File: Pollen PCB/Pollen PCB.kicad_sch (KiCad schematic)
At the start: 4 parts, among them U1 DS18B20, U2 Pico, U3 GY-NEO6MV2

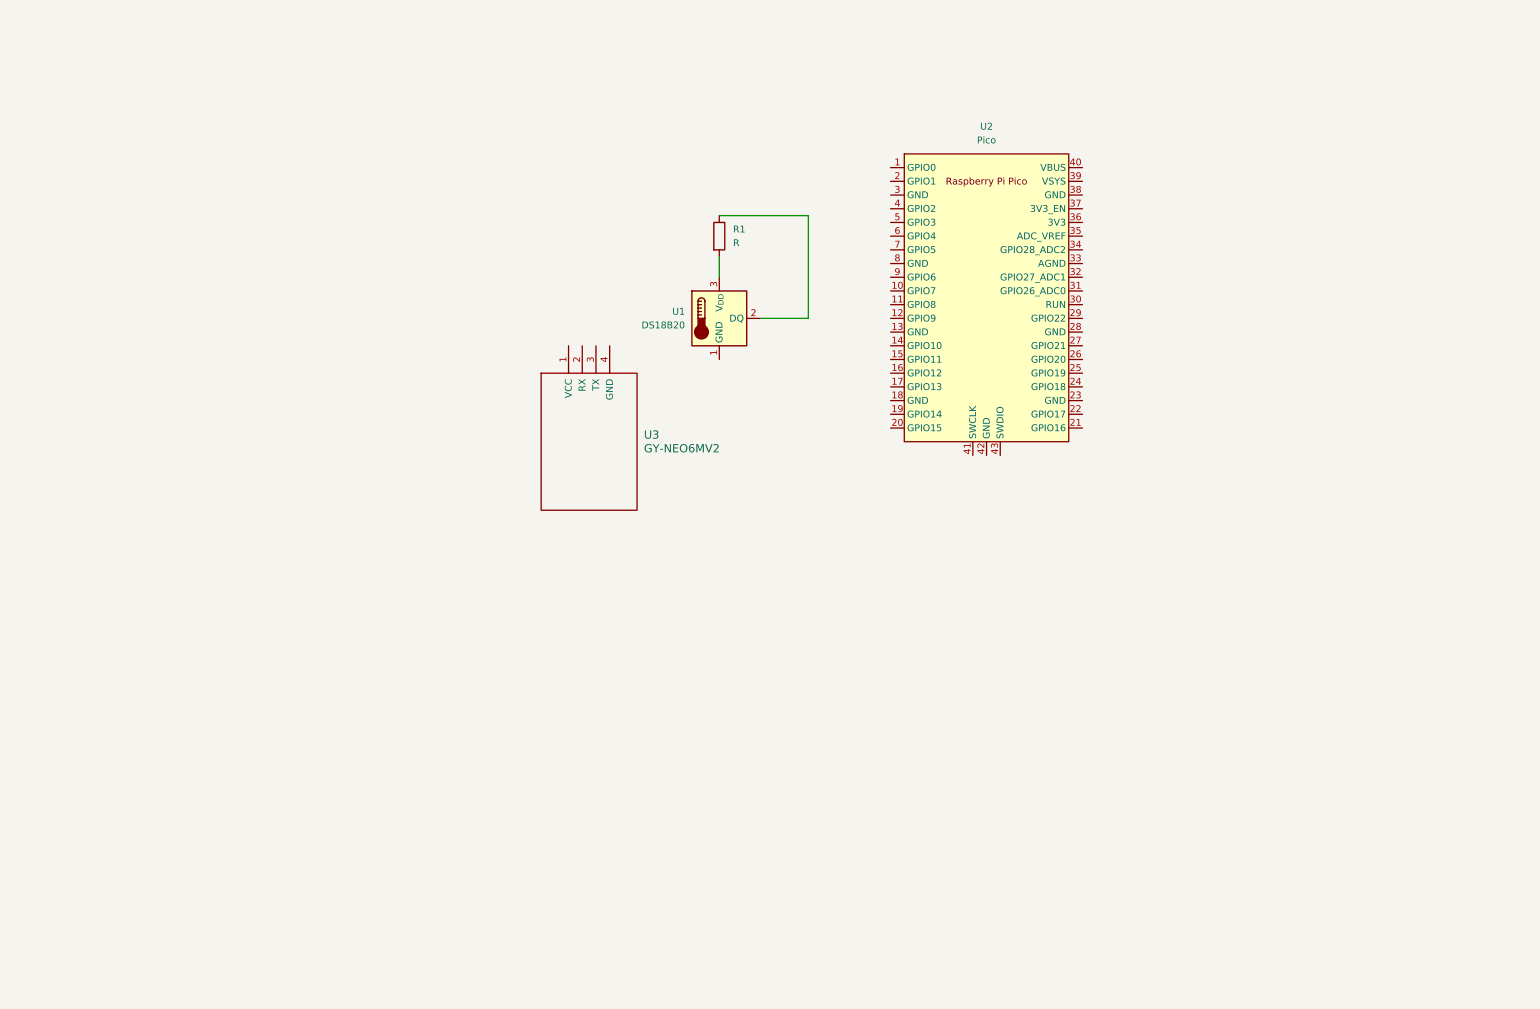
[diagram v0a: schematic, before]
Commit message: Start drawing the schematic
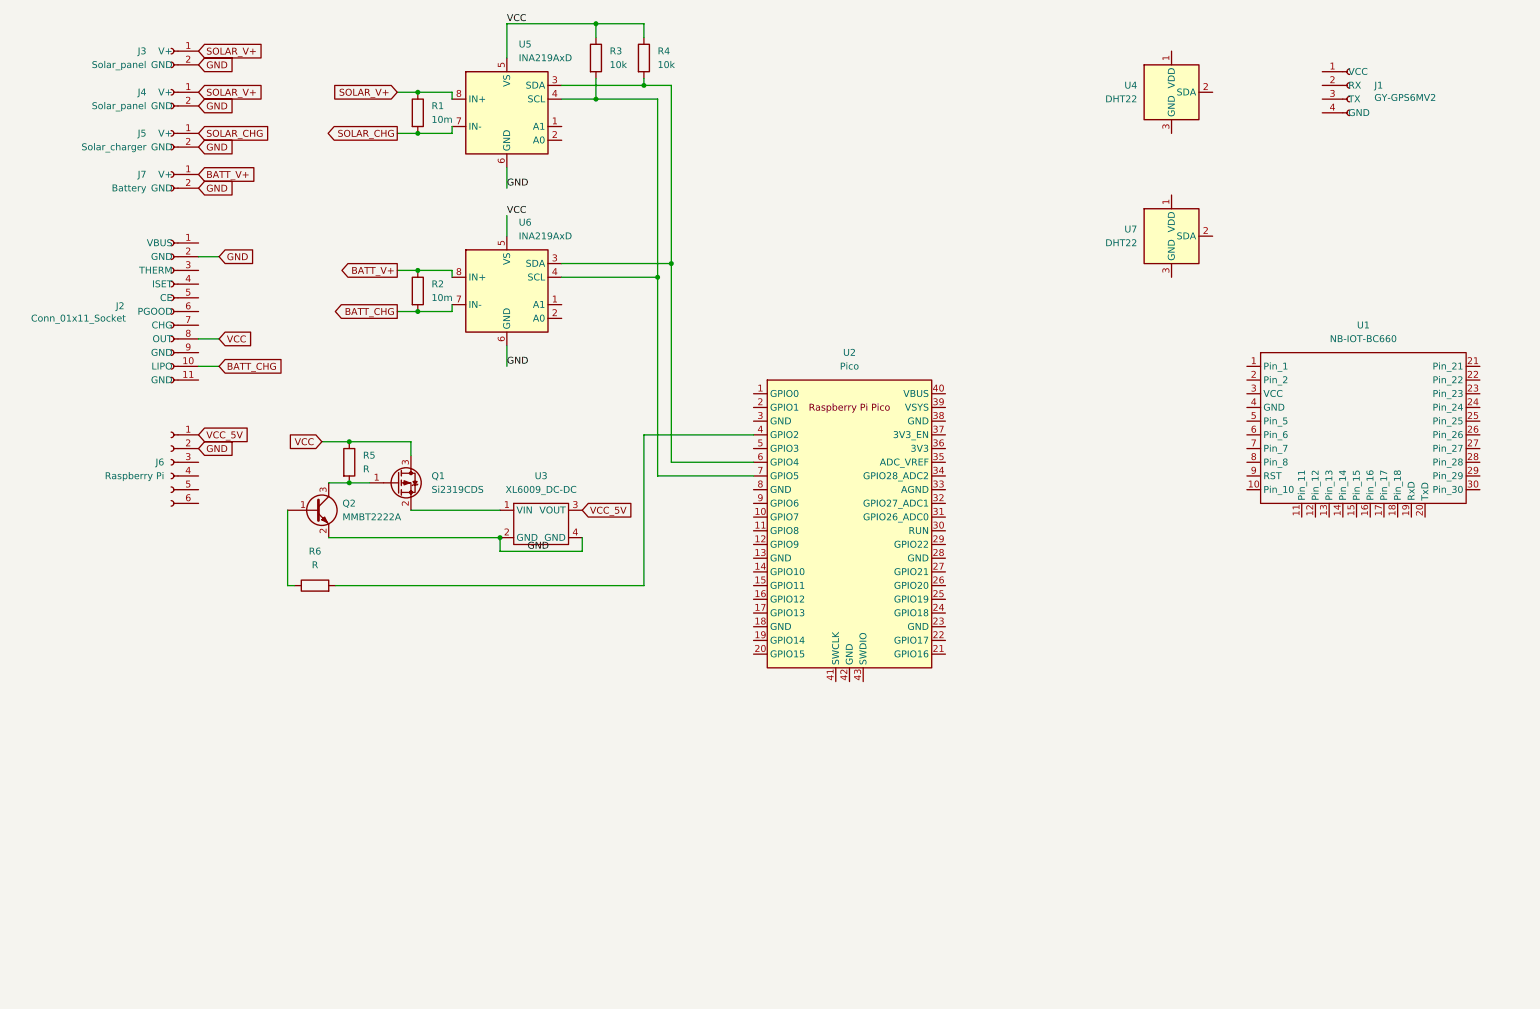
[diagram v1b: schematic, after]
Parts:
- removed U1: DS18B20, Package_TO_SOT_THT:TO-92_Inline, symbol Sensor_Temperature:DS18B20
- removed U3: GY-NEO6MV2, symbol megasaturnv_custom_components:GY-NEO6MV2
- added J1: GY-GPS6MV2, Connector_PinSocket_2.54mm:PinSocket_1x04_P2.54mm_Vertical, symbol Connector:Conn_01x04_Socket
- added J2: Conn_01x11_Socket, Connector_PinSocket_2.54mm:PinSocket_1x11_P2.54mm_Vertical, symbol Connector:Conn_01x11_Socket
- added J3, J4: Solar_panel, Connector_PinSocket_2.54mm:PinSocket_1x02_P2.54mm_Vertical, symbol Connector:Conn_01x02_Socket
- added J5: Solar_charger, Connector_PinSocket_2.54mm:PinSocket_1x02_P2.54mm_Vertical, symbol Connector:Conn_01x02_Socket
- added J6: Raspberry Pi, Connector_PinSocket_2.54mm:PinSocket_1x06_P2.54mm_Vertical, symbol Connector:Conn_01x06_Socket
- added J7: Battery, Connector_PinSocket_2.54mm:PinSocket_1x02_P2.54mm_Vertical, symbol Connector:Conn_01x02_Socket
- added Q1: Si2319CDS, Package_TO_SOT_SMD:SOT-23, symbol Transistor_FET:Si2319CDS
- added Q2: MMBT2222A, Package_TO_SOT_SMD:SOT-23, symbol Transistor_BJT:MMBT2222A
- added R2: 10m, symbol Device:R
- added R3, R4: 10k, symbol Device:R
- added R5, R6: R, symbol Device:R
- added U1: NB-IOT-BC660, Custom_Components:NB-IOT-BC660, symbol Custom_Components:BC660_Olimex_module
- added U3: XL6009_DC-DC, Custom_Components:XL6009_DC-DC, symbol Custom_Components:XL6009_DC-DC
- added U4, U7: DHT22, Sensor:ASAIR_AM2302_P2.54mm_Vertical, symbol Sensor:AM2302
- added U5, U6: INA219AxD, Package_SO:SOIC-8_3.9x4.9mm_P1.27mm, symbol Sensor_Energy:INA219AxD
- R1: value R -> 10m; footprint Resistor_THT:R_Axial_DIN0204_L3.6mm_D1.6mm_P7.62mm_Horizontal -> (none)
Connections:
- net SOLAR_V+: now reaches R1.1
- net SOLAR_V+: now also J3.1 (V+), J4.1 (V+), U5.8 (IN+)
- net SOLAR_CHG: now reaches R1.2
- net SOLAR_CHG: now also J5.1 (V+), U5.7 (IN-)
- net at U2.4 (GPIO2): now also R6.2
- net at U2.6 (GPIO4): now also R4.2, U5.3 (SDA), U6.3 (SDA)
- net at U2.7 (GPIO5): now also R3.2, U5.4 (SCL), U6.4 (SCL)
- new net: Q1.1 (G), Q2.3 (C), R5.2
- new net: Q1.2 (S), U3.1 (VIN)
- new net: U7.3 (GND), U7.4 (GND)
- new net: U4.3 (GND), U4.4 (GND)
- new net: Q2.1 (B), R6.1
- new net BATT_CHG: J2.10 (LIPO), R2.2, U6.7 (IN-)
- new net BATT_V+: J7.1 (V+), R2.1, U6.8 (IN+)
- new net GND: J2.2 (GND), J3.2 (GND), J4.2 (GND), J5.2 (GND), J6.2 (Pin_2), J7.2 (GND), Q2.2 (E), U3.2 (GND), U3.4 (GND), U5.6 (GND), U6.6 (GND)
- new net VCC: J2.8 (OUT), Q1.3 (D), R3.1, R4.1, R5.1, U5.5 (VS), U6.5 (VS)
- new net VCC_5V: J6.1 (Pin_1), U3.3 (VOUT)
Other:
- moved on the sheet: U2

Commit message: Schematic v1.0
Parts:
- added C1: 100nF, Capacitor_THT:C_Axial_L5.1mm_D3.1mm_P10.00mm_Horizontal, symbol Device:C
- added Q3: MMBT2222A, Package_TO_SOT_SMD:SOT-23, symbol Transistor_BJT:MMBT2222A
- added Q4: Si2319CDS, Package_TO_SOT_SMD:SOT-23, symbol Transistor_FET:Si2319CDS
- added R7: 1k, symbol Device:R
- added R8: 10k, symbol Device:R
- J2: value Conn_01x11_Socket -> Adafruit Charge Controller
- R5: value R -> 10k
- R6: value R -> 1k
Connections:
- net VCC_5V is gone; now on net +5V: J6.1 (Pin_1), U3.3 (VOUT)
- net GND: now also J1.4 (GND), J2.11 (GND), J2.9 (GND), U1.4 (GND), U2.13 (GND), U2.18 (GND), U2.23 (GND), U2.28 (GND), U2.3 (GND), U2.38 (GND), U2.8 (GND), U4.3 (GND), U4.4 (GND), U5.1 (A1), U5.2 (A0), U6.1 (A1), U7.3 (GND), U7.4 (GND), C1.2, Q3.2 (E)
- net +5V: now reaches J1.1 (VCC)
- net GPS_RX: now reaches J1.2 (RX)
- net GPS_RX: now also U2.11 (GPIO8)
- net GPS_TX: now reaches J1.3 (TX)
- net GPS_TX: now also U2.12 (GPIO9)
- net NB-IOT_RX: now reaches U1.19 (RxD)
- net NB-IOT_RX: now also U2.1 (GPIO0)
- net NB-IOT_TX: now reaches U1.20 (TxD)
- net NB-IOT_TX: now also U2.2 (GPIO1)
- net +3V3: now reaches U1.3 (VCC)
- net +3V3: now also R3.1, R4.1, U2.36 (3V3), U5.5 (VS), U6.2 (A0), U6.5 (VS), C1.1, Q4.3 (D), R8.1
- net NB-IOT_RST: now reaches U1.9 (RST)
- net NB-IOT_RST: now also U2.9 (GPIO6)
- net SDA: now reaches U2.6 (GPIO4), U5.3 (SDA), U6.3 (SDA)
- net SDA: now also R3.2; no longer R4.2
- net SCL: now reaches U2.7 (GPIO5), U5.4 (SCL), U6.4 (SCL)
- net SCL: now also R4.2; no longer R3.2
- net CHARGER_PGOOD: now reaches J2.6 (PGOOD)
- net CHARGER_PGOOD: now also U2.15 (GPIO11)
- net CHARGER_CHG: now reaches J2.7 (CHG)
- net CHARGER_CHG: now also U2.14 (GPIO10)
- net +3V3_SENSOR: now reaches U7.1 (VDD)
- net +3V3_SENSOR: now also U4.1 (VDD), Q4.2 (S)
- net DHT_2: now reaches U7.2 (SDA)
- net DHT_2: now also U2.20 (GPIO15)
- net RPI_MOSI: now reaches J6.3 (Pin_3)
- net RPI_MOSI: now also U2.25 (GPIO19)
- net RPI_MISO: now reaches J6.4 (Pin_4)
- net RPI_MISO: now also U2.21 (GPIO16)
- net RPI_SCK: now reaches J6.5 (Pin_5)
- net RPI_SCK: now also U2.24 (GPIO18)
- net RPI_CS: now reaches J6.6 (Pin_6)
- net RPI_CS: now also U2.22 (GPIO17)
- net DHT_1: now reaches U4.2 (SDA)
- net DHT_1: now also U2.19 (GPIO14)
- net at Q2.1 (B): now also R6.2; no longer R6.1
- net 3V3_SENSOR_CONTROL: now reaches U2.4 (GPIO2)
- net 3V3_SENSOR_CONTROL: now also R7.1; no longer R6.2
- net +BATT: now reaches U2.39 (VSYS)
- net +BATT: now also J2.8 (OUT), Q1.3 (D), R5.1
- net 5V_CONTROL: now reaches U2.5 (GPIO3)
- net 5V_CONTROL: now also R6.1
- net BATT_CHG renamed CHARGER_LIPO
- net BATT_V+ renamed BATTERY+
- net SOLAR_CHG renamed CHARGER_V+
- removed net VCC: J2.8 (OUT), Q1.3 (D), R3.1, R4.1, R5.1, U5.5 (VS), U6.5 (VS)
- new net: Q3.3 (C), Q4.1 (G), R8.2
- new net: Q3.1 (B), R7.2
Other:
- note added: "Energy harvesting and monitoring"
- note added: "GPS module"
- note added: "Microcontroller and NB IoT network"
- note added: "Raspberry Pi"
- note added: "Sensors"
- company: (none) -> Mau & Botond
- title: (none) -> Data Collector Controller
- moved on the sheet: J1, J2, J3, J4, J5, J7, Q1, Q2, R1, R2, R3, R4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

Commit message: Updated PCB + footprints
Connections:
- net RPI_CS: now also J6.5 (Pin_5); no longer J6.6 (Pin_6)
- net RPI_MISO: now also J6.6 (Pin_6); no longer J6.4 (Pin_4)
- net RPI_SCK: now also J6.4 (Pin_4); no longer J6.5 (Pin_5)
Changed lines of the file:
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@@
 		)
 	)
-	(label "RPI_CS"
+	(label "RPI_MISO"
 		(at 48.26 181.61 180)
 		(fields_autoplaced yes)
@@
 		)
 	)
-	(label "RPI_SCK"
+	(label "RPI_CS"
 		(at 48.26 179.07 180)
 		(fields_autoplaced yes)
@@
 		)
 	)
-	(label "RPI_MISO"
+	(label "RPI_SCK"
 		(at 48.26 176.53 180)
 		(fields_autoplaced yes)

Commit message: Update PCB
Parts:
- added J8: RPi power, Connector_PinSocket_2.54mm:PinSocket_1x02_P2.54mm_Vertical, symbol Connector:Conn_01x02_Socket
- added R10: 10k, Resistor_SMD:R_1206_3216Metric_Pad1.30x1.75mm_HandSolder, symbol Device:R
- added R9: 5k1, Resistor_SMD:R_1206_3216Metric_Pad1.30x1.75mm_HandSolder, symbol Device:R
- C1: footprint Capacitor_THT:C_Axial_L5.1mm_D3.1mm_P10.00mm_Horizontal -> Capacitor_SMD:C_1206_3216Metric_Pad1.33x1.80mm_HandSolder
- J6: footprint Connector_PinSocket_2.54mm:PinSocket_1x06_P2.54mm_Vertical -> Connector_PinSocket_2.54mm:PinSocket_1x04_P2.54mm_Vertical; symbol Connector:Conn_01x06_Socket -> Connector:Conn_01x04_Socket
- R1, R2: value 10m -> 100m; footprint (none) -> Resistor_SMD:R_2512_6332Metric_Pad1.40x3.35mm_HandSolder
- R3, R4, R5, R6, R7, R8: footprint (none) -> Resistor_SMD:R_1206_3216Metric_Pad1.30x1.75mm_HandSolder
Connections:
- net +5V: now also J8.2 (V+); no longer J6.1 (Pin_1)
- net 3V3_SENSOR_CONTROL: now also U2.26 (GPIO20); no longer U2.4 (GPIO2)
- net BATTERY+: now also J7.2 (GND), R2.2, U6.7 (IN-); no longer J7.1 (V+), R2.1, U6.8 (IN+)
- net CHARGER_CHG: now also U2.29 (GPIO22); no longer U2.14 (GPIO10)
- net CHARGER_LIPO: now also R2.1, U6.8 (IN+); no longer R2.2, U6.7 (IN-)
- net CHARGER_PGOOD: now also U2.27 (GPIO21); no longer U2.15 (GPIO11)
- net CHARGER_V+: now also J5.2 (GND); no longer J5.1 (V+)
- net DHT_1: now also U2.17 (GPIO13); no longer U2.19 (GPIO14)
- net GND: now also J3.1 (V+), J4.1 (V+), J5.1 (V+), J7.1 (V+), J8.1 (GND), R10.2; no longer J3.2 (GND), J4.2 (GND), J5.2 (GND), J6.2 (Pin_2), J7.2 (GND)
- net GPS_TX: now also R10.1, R9.2; no longer J1.3 (TX)
- net NB-IOT_RST: now also U2.4 (GPIO2); no longer U2.9 (GPIO6)
- net RPI_CS: now also J6.3 (Pin_3); no longer J6.5 (Pin_5)
- net RPI_MISO: now also J6.4 (Pin_4); no longer J6.6 (Pin_6)
- net RPI_MOSI: now also J6.1 (Pin_1); no longer J6.3 (Pin_3)
- net RPI_SCK: now also J6.2 (Pin_2); no longer J6.4 (Pin_4)
- net SOLAR_V+: now also J3.2 (GND), J4.2 (GND); no longer J3.1 (V+), J4.1 (V+)
- net GPS_RX: no longer names the net of J1.2 (RX)
- net GPS_RX: no longer U2.11 (GPIO8)
- new net: J1.3 (TX), R9.1
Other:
- moved on the sheet: J1, R1, R2
